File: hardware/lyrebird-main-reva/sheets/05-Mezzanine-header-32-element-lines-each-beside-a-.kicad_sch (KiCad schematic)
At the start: 6 parts, among them J2 Mezzanine 2x40

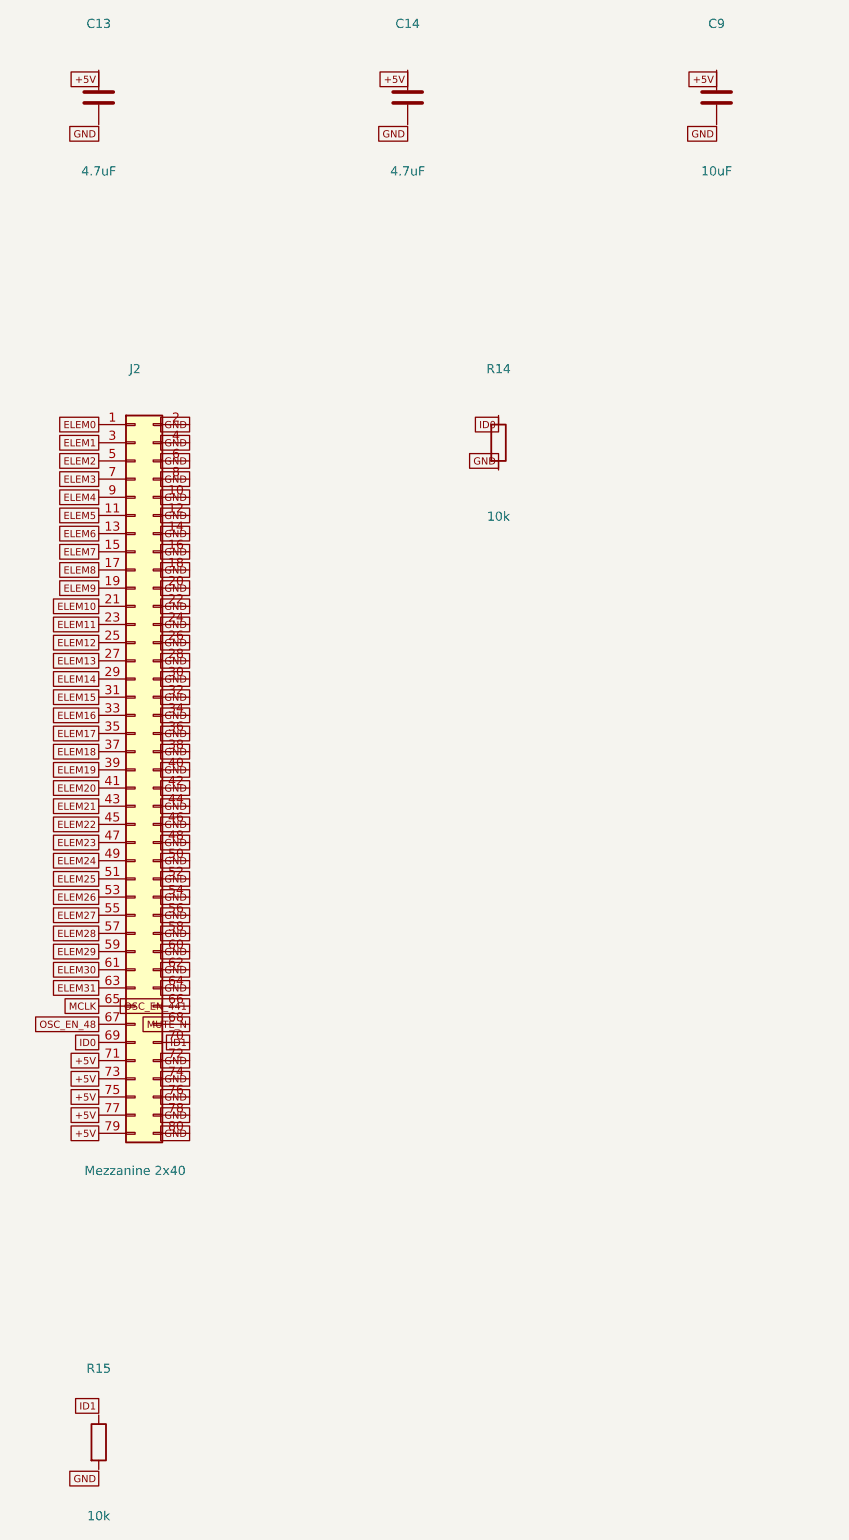
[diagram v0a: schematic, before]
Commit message: Regenerate the schematics, which were eleven days behind the netlists
The sheets and both PDFs dated 13 September against netlists from
today. They showed a board with USB bus power, a charge pump on the
analog module, no JTAG series protection, no oscillator pull-downs and
none of the footprint corrections -- a board that has not existed for
some time. Anyone opening them to review the design would have been
reviewing the wrong one, which is worse than having no schematic.

Regenerated from the current netlists: the main board goes from 8
sheets to 11, picking up the wall-wart input and the inverter, and the
module from 6 to 9 while losing the charge pump entirely. Both PDFs
rebuilt through kicad-cli, one page per sheet.

Nothing regenerated them because nothing was watching. The netlist
generators are run constantly and the views derived from them are not,
so they drift silently and there is no check that notices.

Co-Authored-By: Claude Opus 5 <noreply@anthropic.com>
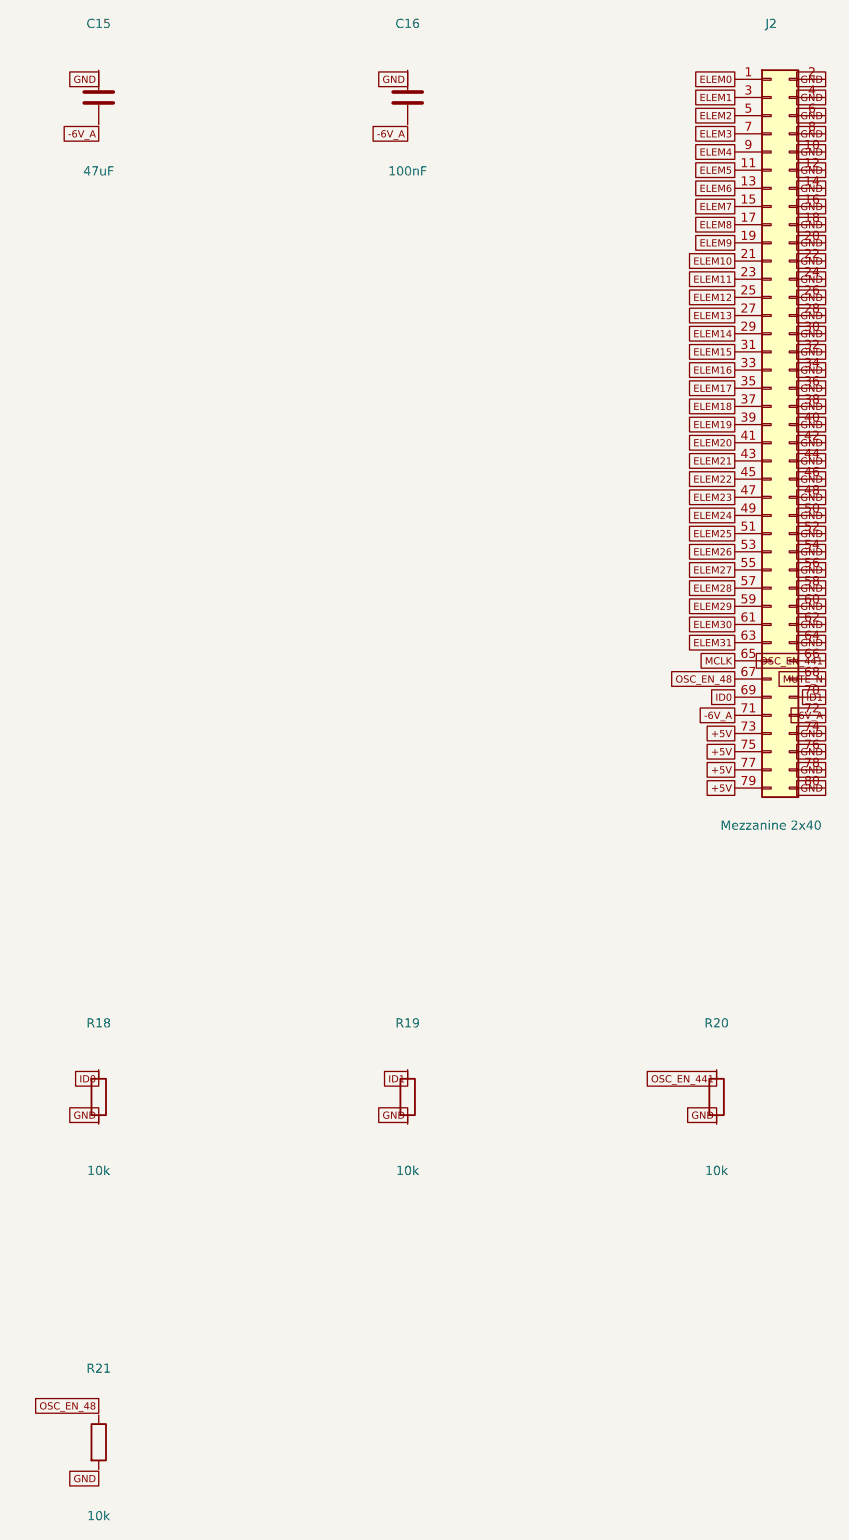
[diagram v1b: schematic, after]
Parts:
- added R21: 10k, symbol Device:R
- C15: renamed from C13; value 4.7uF -> 47uF
- C16: renamed from C14; value 4.7uF -> 100nF
- J2: renamed from C9; value 10uF -> Mezzanine 2x40; symbol Device:C -> Connector_Generic:Conn_02x40_Odd_Even
- R18: renamed from J2; value Mezzanine 2x40 -> 10k; symbol Connector_Generic:Conn_02x40_Odd_Even -> Device:R
- renumbered R14 to R19, R15 to R20
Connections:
- net +5V: now also J2.73 (Pin_73), J2.75 (Pin_75), J2.77 (Pin_77), J2.79 (Pin_79); no longer R18.71 (Pin_71), R18.73 (Pin_73), R18.75 (Pin_75), R18.77 (Pin_77), R18.79 (Pin_79)
- net ELEM0: now also J2.1 (Pin_1); no longer R18.1 (Pin_1)
- net ELEM1: now also J2.3 (Pin_3); no longer R18.3 (Pin_3)
- net ELEM10: now also J2.21 (Pin_21); no longer R18.21 (Pin_21)
- net ELEM11: now also J2.23 (Pin_23); no longer R18.23 (Pin_23)
- net ELEM12: now also J2.25 (Pin_25); no longer R18.25 (Pin_25)
- net ELEM13: now also J2.27 (Pin_27); no longer R18.27 (Pin_27)
- net ELEM14: now also J2.29 (Pin_29); no longer R18.29 (Pin_29)
- net ELEM15: now also J2.31 (Pin_31); no longer R18.31 (Pin_31)
- net ELEM16: now also J2.33 (Pin_33); no longer R18.33 (Pin_33)
- net ELEM17: now also J2.35 (Pin_35); no longer R18.35 (Pin_35)
- net ELEM18: now also J2.37 (Pin_37); no longer R18.37 (Pin_37)
- net ELEM19: now also J2.39 (Pin_39); no longer R18.39 (Pin_39)
- net ELEM2: now also J2.5 (Pin_5); no longer R18.5 (Pin_5)
- net ELEM20: now also J2.41 (Pin_41); no longer R18.41 (Pin_41)
- net ELEM21: now also J2.43 (Pin_43); no longer R18.43 (Pin_43)
- net ELEM22: now also J2.45 (Pin_45); no longer R18.45 (Pin_45)
- net ELEM23: now also J2.47 (Pin_47); no longer R18.47 (Pin_47)
- net ELEM24: now also J2.49 (Pin_49); no longer R18.49 (Pin_49)
- net ELEM25: now also J2.51 (Pin_51); no longer R18.51 (Pin_51)
- net ELEM26: now also J2.53 (Pin_53); no longer R18.53 (Pin_53)
- net ELEM27: now also J2.55 (Pin_55); no longer R18.55 (Pin_55)
- net ELEM28: now also J2.57 (Pin_57); no longer R18.57 (Pin_57)
- net ELEM29: now also J2.59 (Pin_59); no longer R18.59 (Pin_59)
- net ELEM3: now also J2.7 (Pin_7); no longer R18.7 (Pin_7)
- net ELEM30: now also J2.61 (Pin_61); no longer R18.61 (Pin_61)
- net ELEM31: now also J2.63 (Pin_63); no longer R18.63 (Pin_63)
- net ELEM4: now also J2.9 (Pin_9); no longer R18.9 (Pin_9)
- net ELEM5: now also J2.11 (Pin_11); no longer R18.11 (Pin_11)
- net ELEM6: now also J2.13 (Pin_13); no longer R18.13 (Pin_13)
- net ELEM7: now also J2.15 (Pin_15); no longer R18.15 (Pin_15)
- net ELEM8: now also J2.17 (Pin_17); no longer R18.17 (Pin_17)
- net ELEM9: now also J2.19 (Pin_19); no longer R18.19 (Pin_19)
- net GND: now also J2.10 (Pin_10), J2.12 (Pin_12), J2.14 (Pin_14), J2.16 (Pin_16), J2.18 (Pin_18), J2.2 (Pin_2), J2.20 (Pin_20), J2.22 (Pin_22), J2.24 (Pin_24), J2.26 (Pin_26), J2.28 (Pin_28), J2.30 (Pin_30), J2.32 (Pin_32), J2.34 (Pin_34), J2.36 (Pin_36), J2.38 (Pin_38), J2.4 (Pin_4), J2.40 (Pin_40), J2.42 (Pin_42), J2.44 (Pin_44), J2.46 (Pin_46), J2.48 (Pin_48), J2.50 (Pin_50), J2.52 (Pin_52), J2.54 (Pin_54), J2.56 (Pin_56), J2.58 (Pin_58), J2.6 (Pin_6), J2.60 (Pin_60), J2.62 (Pin_62), J2.64 (Pin_64), J2.74 (Pin_74), J2.76 (Pin_76), J2.78 (Pin_78), J2.8 (Pin_8), J2.80 (Pin_80); no longer R18.10 (Pin_10), R18.12 (Pin_12), R18.14 (Pin_14), R18.16 (Pin_16), R18.18 (Pin_18), R18.2 (Pin_2), R18.20 (Pin_20), R18.22 (Pin_22), R18.24 (Pin_24), R18.26 (Pin_26), R18.28 (Pin_28), R18.30 (Pin_30), R18.32 (Pin_32), R18.34 (Pin_34), R18.36 (Pin_36), R18.38 (Pin_38), R18.4 (Pin_4), R18.40 (Pin_40), R18.42 (Pin_42), R18.44 (Pin_44), R18.46 (Pin_46), R18.48 (Pin_48), R18.50 (Pin_50), R18.52 (Pin_52), R18.54 (Pin_54), R18.56 (Pin_56), R18.58 (Pin_58), R18.6 (Pin_6), R18.60 (Pin_60), R18.62 (Pin_62), R18.64 (Pin_64), R18.72 (Pin_72), R18.74 (Pin_74), R18.76 (Pin_76), R18.78 (Pin_78), R18.8 (Pin_8), R18.80 (Pin_80)
- net ID0: now also J2.69 (Pin_69); no longer R18.69 (Pin_69)
- net ID1: now also J2.70 (Pin_70); no longer R18.70 (Pin_70)
- net MCLK: now also J2.65 (Pin_65); no longer R18.65 (Pin_65)
- net MUTE_N: now also J2.68 (Pin_68); no longer R18.68 (Pin_68)
- net OSC_EN_441: now also J2.66 (Pin_66); no longer R18.66 (Pin_66)
- net OSC_EN_48: now also J2.67 (Pin_67); no longer R18.67 (Pin_67)
- new net -6V_A: J2.71 (Pin_71), J2.72 (Pin_72)
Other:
- moved on the sheet: R19, R20

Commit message: Act on the schematic validation: three faults and the core-rail guard
**The SuperSpeed pairs were wired backwards, and are now not wired.**
USB_SSRX_P/N were the only multi-node nets on the board with an INPUT at
every pin -- the receptacle's SSRX pins are inputs and so are the
bridge's RIDP/RIDN, so nothing drove them, and the transmit pair was
mirrored the same way. The comment asserted a crossover inside the cable
as fact and reasoned from it; USB 3.0 cables have no crossover.
SuperSpeed would never have trained and the link would have fallen back
to 480 Mb/s silently -- which is the speed 0014 chose on purpose, since
no galvanic isolator exists above USB 2.0. So the pairs are removed
rather than corrected, which also retires the hardest constraint in this
board's layout. How to wire them correctly if they ever come back is
recorded where they were.

**The inverting converter had no input capacitor across its own
terminals.** Nothing spanned +12V and -6V_A, and U7's GND pin *is*
-6V_A, so the loop its switching current actually takes was unbypassed
-- the input caps near U5 are referenced to system ground and are not in
that loop at all. This is the third fault found in U7 and all three are
the same mistake: reasoning about it as though its ground were the
board's.

**The translator's output enables are tied low against an explicit
datasheet instruction**, and the fix is sequencing rather than a pull-up.
SCES576I says OE must be pulled up to VCCA and not enabled until both
supplies are stable; a pull-up is not available here because nothing on
the module could pull it down -- no spare mezzanine pin, and MUTE_N has
the wrong polarity. Instead VCC(A) is made the last rail to arrive:
10 uF on U9's SET gives 573 ms against 359 ms for VCC(B), so the enable
cannot precede the supply it switches to. It costs nothing, because that
rail feeds the translator's reference supply and nothing else.

**The core rail now has a guard, and it needed two attempts.** The
existing as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
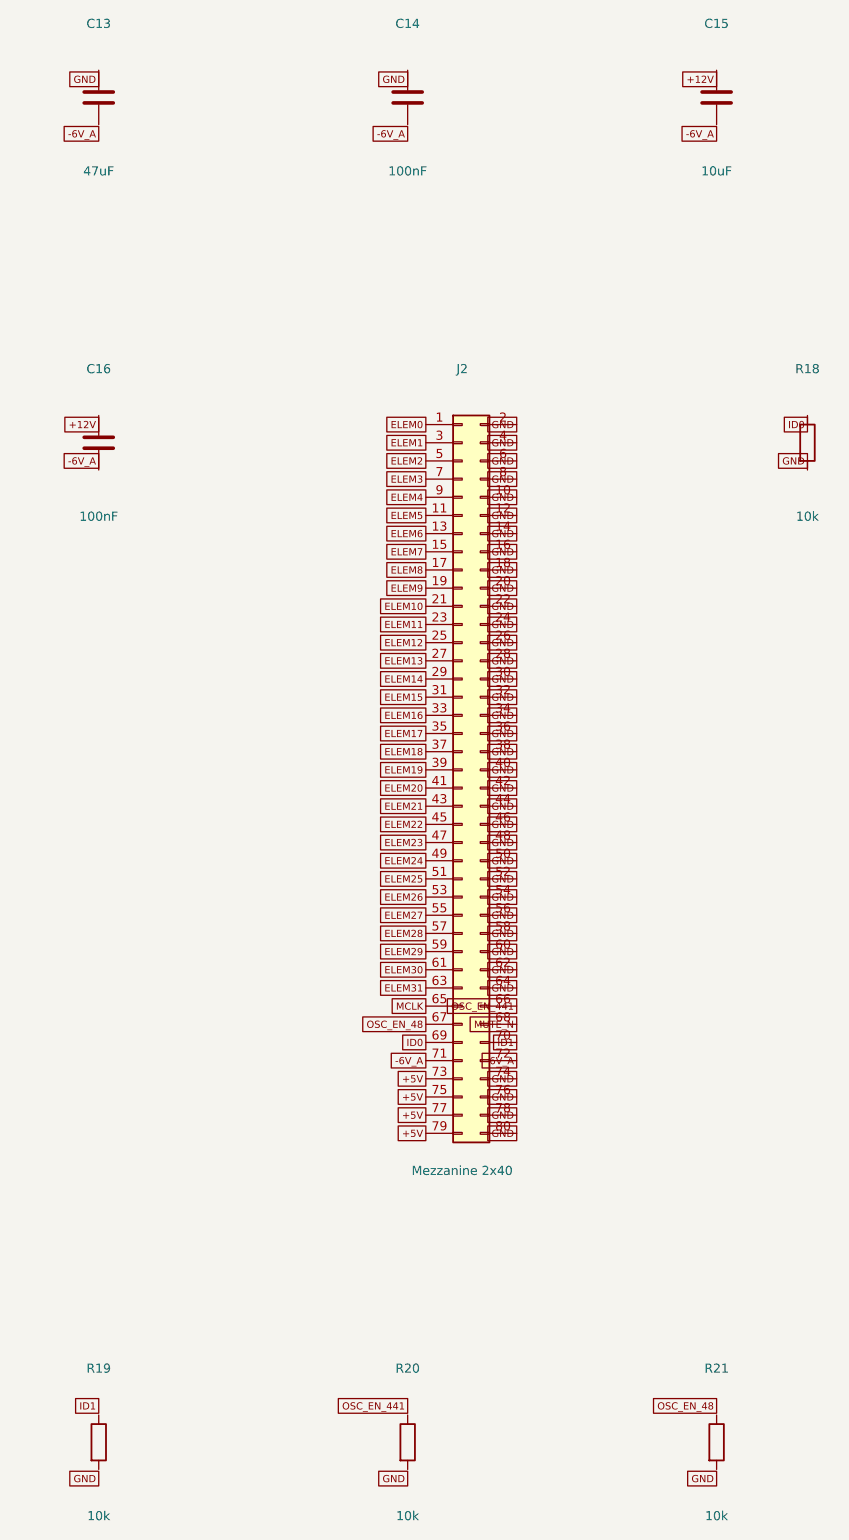
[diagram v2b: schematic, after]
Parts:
- added R20, R21: 10k, symbol Device:R
- C15: renamed from J2; value Mezzanine 2x40 -> 10uF; symbol Connector_Generic:Conn_02x40_Odd_Even -> Device:C
- C16: renamed from R18; value 10k -> 100nF; symbol Device:R -> Device:C
- J2: renamed from R19; value 10k -> Mezzanine 2x40; symbol Device:R -> Connector_Generic:Conn_02x40_Odd_Even
- renumbered C15 to C13, C16 to C14, R20 to R18, R21 to R19
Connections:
- net +5V: now also J2.73 (Pin_73), J2.75 (Pin_75), J2.77 (Pin_77), J2.79 (Pin_79); no longer C15.73 (Pin_73), C15.75 (Pin_75), C15.77 (Pin_77), C15.79 (Pin_79)
- net -6V_A: now also J2.71 (Pin_71), J2.72 (Pin_72); no longer C15.71 (Pin_71), C15.72 (Pin_72)
- net ELEM0: now also J2.1 (Pin_1); no longer C15.1 (Pin_1)
- net ELEM1: now also J2.3 (Pin_3); no longer C15.3 (Pin_3)
- net ELEM10: now also J2.21 (Pin_21); no longer C15.21 (Pin_21)
- net ELEM11: now also J2.23 (Pin_23); no longer C15.23 (Pin_23)
- net ELEM12: now also J2.25 (Pin_25); no longer C15.25 (Pin_25)
- net ELEM13: now also J2.27 (Pin_27); no longer C15.27 (Pin_27)
- net ELEM14: now also J2.29 (Pin_29); no longer C15.29 (Pin_29)
- net ELEM15: now also J2.31 (Pin_31); no longer C15.31 (Pin_31)
- net ELEM16: now also J2.33 (Pin_33); no longer C15.33 (Pin_33)
- net ELEM17: now also J2.35 (Pin_35); no longer C15.35 (Pin_35)
- net ELEM18: now also J2.37 (Pin_37); no longer C15.37 (Pin_37)
- net ELEM19: now also J2.39 (Pin_39); no longer C15.39 (Pin_39)
- net ELEM2: now also J2.5 (Pin_5); no longer C15.5 (Pin_5)
- net ELEM20: now also J2.41 (Pin_41); no longer C15.41 (Pin_41)
- net ELEM21: now also J2.43 (Pin_43); no longer C15.43 (Pin_43)
- net ELEM22: now also J2.45 (Pin_45); no longer C15.45 (Pin_45)
- net ELEM23: now also J2.47 (Pin_47); no longer C15.47 (Pin_47)
- net ELEM24: now also J2.49 (Pin_49); no longer C15.49 (Pin_49)
- net ELEM25: now also J2.51 (Pin_51); no longer C15.51 (Pin_51)
- net ELEM26: now also J2.53 (Pin_53); no longer C15.53 (Pin_53)
- net ELEM27: now also J2.55 (Pin_55); no longer C15.55 (Pin_55)
- net ELEM28: now also J2.57 (Pin_57); no longer C15.57 (Pin_57)
- net ELEM29: now also J2.59 (Pin_59); no longer C15.59 (Pin_59)
- net ELEM3: now also J2.7 (Pin_7); no longer C15.7 (Pin_7)
- net ELEM30: now also J2.61 (Pin_61); no longer C15.61 (Pin_61)
- net ELEM31: now also J2.63 (Pin_63); no longer C15.63 (Pin_63)
- net ELEM4: now also J2.9 (Pin_9); no longer C15.9 (Pin_9)
- net ELEM5: now also J2.11 (Pin_11); no longer C15.11 (Pin_11)
- net ELEM6: now also J2.13 (Pin_13); no longer C15.13 (Pin_13)
- net ELEM7: now also J2.15 (Pin_15); no longer C15.15 (Pin_15)
- net ELEM8: now also J2.17 (Pin_17); no longer C15.17 (Pin_17)
- net ELEM9: now also J2.19 (Pin_19); no longer C15.19 (Pin_19)
- net GND: now also J2.10 (Pin_10), J2.12 (Pin_12), J2.14 (Pin_14), J2.16 (Pin_16), J2.18 (Pin_18), J2.2 (Pin_2), J2.20 (Pin_20), J2.22 (Pin_22), J2.24 (Pin_24), J2.26 (Pin_26), J2.28 (Pin_28), J2.30 (Pin_30), J2.32 (Pin_32), J2.34 (Pin_34), J2.36 (Pin_36), J2.38 (Pin_38), J2.4 (Pin_4), J2.40 (Pin_40), J2.42 (Pin_42), J2.44 (Pin_44), J2.46 (Pin_46), J2.48 (Pin_48), J2.50 (Pin_50), J2.52 (Pin_52), J2.54 (Pin_54), J2.56 (Pin_56), J2.58 (Pin_58), J2.6 (Pin_6), J2.60 (Pin_60), J2.62 (Pin_62), J2.64 (Pin_64), J2.74 (Pin_74), J2.76 (Pin_76), J2.78 (Pin_78), J2.8 (Pin_8), J2.80 (Pin_80); no longer C15.10 (Pin_10), C15.12 (Pin_12), C15.14 (Pin_14), C15.16 (Pin_16), C15.18 (Pin_18), C15.2 (Pin_2), C15.20 (Pin_20), C15.22 (Pin_22), C15.24 (Pin_24), C15.26 (Pin_26), C15.28 (Pin_28), C15.30 (Pin_30), C15.32 (Pin_32), C15.34 (Pin_34), C15.36 (Pin_36), C15.38 (Pin_38), C15.4 (Pin_4), C15.40 (Pin_40), C15.42 (Pin_42), C15.44 (Pin_44), C15.46 (Pin_46), C15.48 (Pin_48), C15.50 (Pin_50), C15.52 (Pin_52), C15.54 (Pin_54), C15.56 (Pin_56), C15.58 (Pin_58), C15.6 (Pin_6), C15.60 (Pin_60), C15.62 (Pin_62), C15.64 (Pin_64), C15.74 (Pin_74), C15.76 (Pin_76), C15.78 (Pin_78), C15.8 (Pin_8), C15.80 (Pin_80)
- net ID0: now also J2.69 (Pin_69); no longer C15.69 (Pin_69)
- net ID1: now also J2.70 (Pin_70); no longer C15.70 (Pin_70)
- net MCLK: now also J2.65 (Pin_65); no longer C15.65 (Pin_65)
- net MUTE_N: now also J2.68 (Pin_68); no longer C15.68 (Pin_68)
- net OSC_EN_441: now also J2.66 (Pin_66); no longer C15.66 (Pin_66)
- net OSC_EN_48: now also J2.67 (Pin_67); no longer C15.67 (Pin_67)
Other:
- moved on the sheet: R18
